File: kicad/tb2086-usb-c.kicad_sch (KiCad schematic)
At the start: 11 parts, among them J1 Conn_01x04, U1 SRV05-4

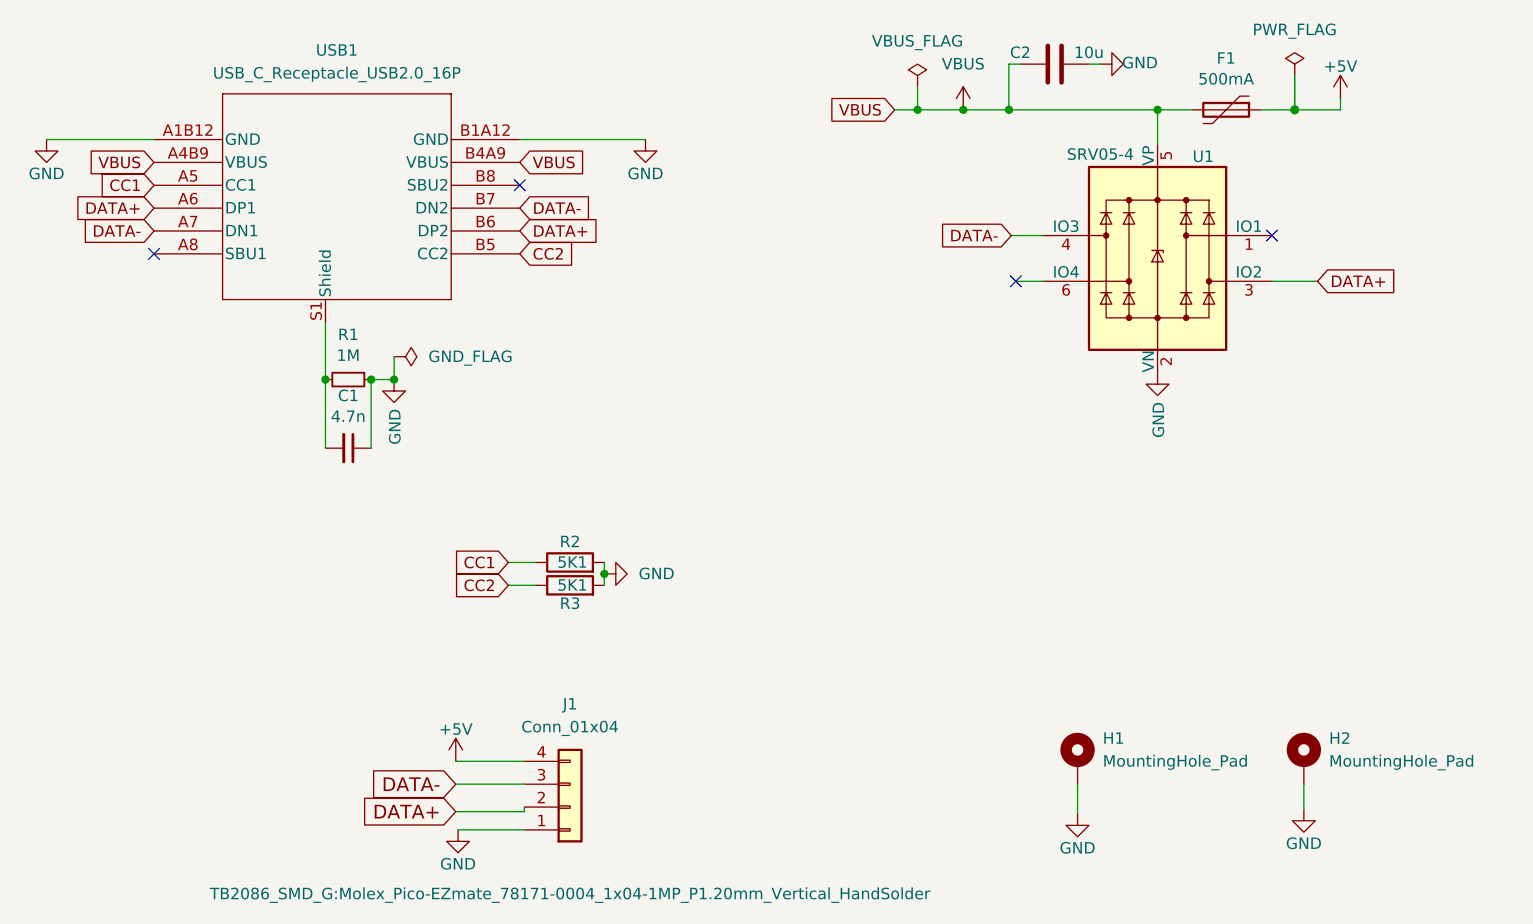
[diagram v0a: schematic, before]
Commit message: replaced ESD protection
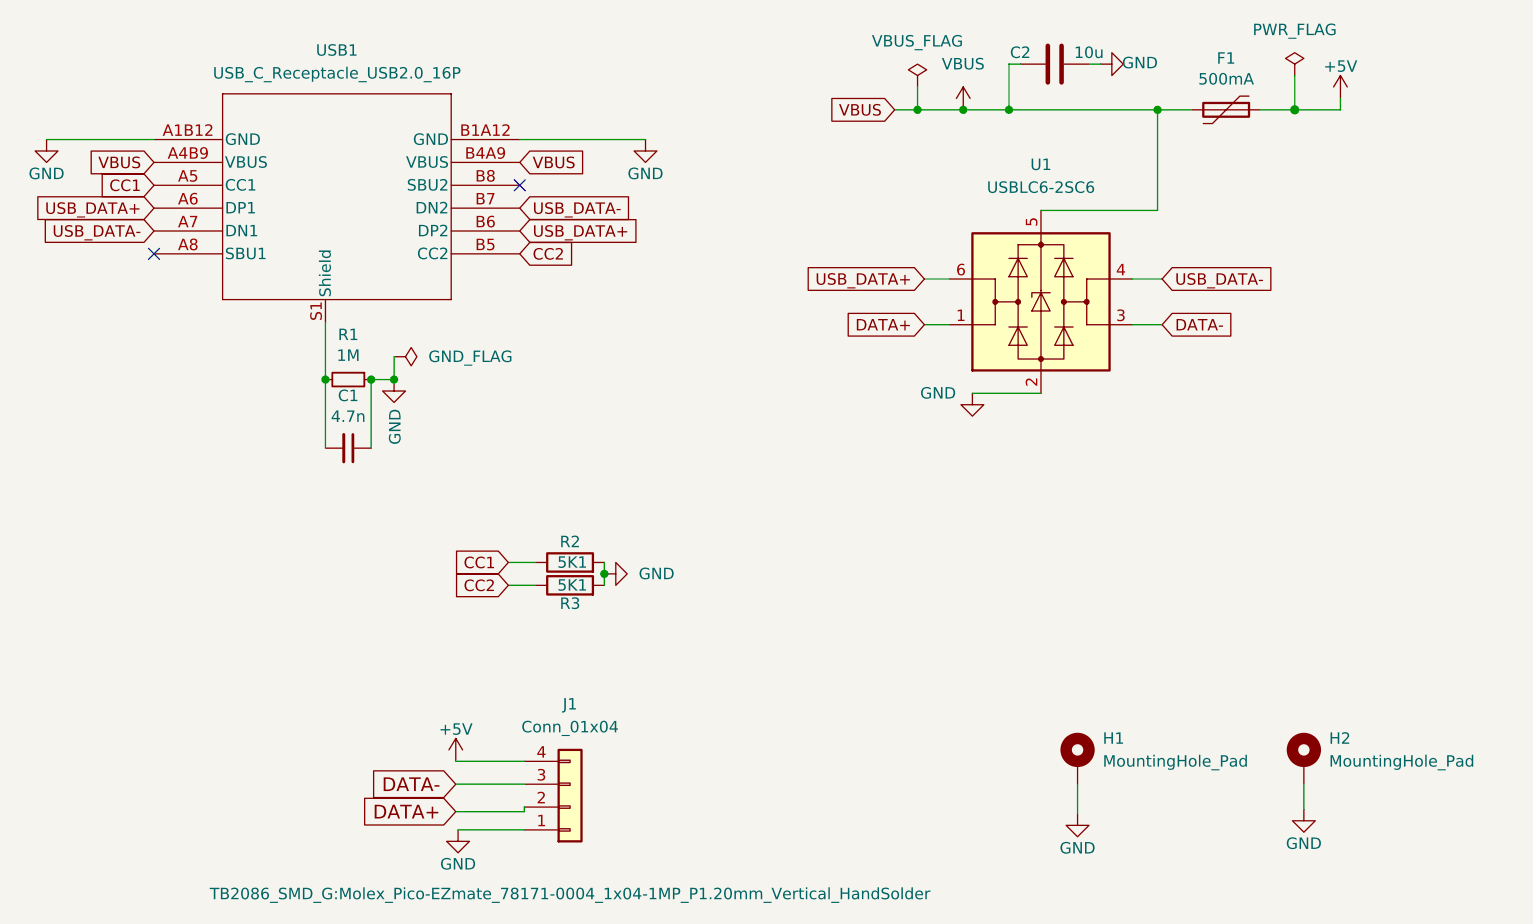
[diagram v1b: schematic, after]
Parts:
- removed U1: SRV05-4, Package_TO_SOT_SMD:SOT-23-6, symbol Power_Protection:SRV05-4
- added U1: USBLC6-2SC6, Package_TO_SOT_SMD:SOT-23-6, symbol Power_Protection:USBLC6-2SC6
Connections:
- net DATA+: now also U1.1 (I/O1); no longer USB1.A6 (DP1), USB1.B6 (DP2)
- net DATA-: now also U1.3 (I/O2); no longer USB1.A7 (DN1), USB1.B7 (DN2)
- net GND: now also U1.2 (GND)
- net VBUS: now also U1.5 (VBUS)
- new net USB_DATA+: U1.6 (I/O1), USB1.A6 (DP1), USB1.B6 (DP2)
- new net USB_DATA-: U1.4 (I/O2), USB1.A7 (DN1), USB1.B7 (DN2)
- no-connect marks 4 -> 2

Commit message: changed footprint (#7)
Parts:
- C2: footprint Capacitor_SMD:C_0603_1608Metric -> Capacitor_SMD:C_0603_1608Metric_Pad1.08x0.95mm_HandSolder
- F1: footprint Fuse:Fuse_0805_2012Metric -> Fuse:Fuse_0805_2012Metric_Pad1.15x1.40mm_HandSolder
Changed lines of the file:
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@@
 			)
 		)
-		(property "Footprint" "Fuse:Fuse_0805_2012Metric"
+		(property "Footprint" "Fuse:Fuse_0805_2012Metric_Pad1.15x1.40mm_HandSolder"
 			(at 145.796 47.498 0)
 			(effects
@@
 			)
 		)
-		(property "Footprint" "Capacitor_SMD:C_0603_1608Metric"
+		(property "Footprint" "Capacitor_SMD:C_0603_1608Metric_Pad1.08x0.95mm_HandSolder"
 			(at 128.016 42.1132 0)
 			(effects
